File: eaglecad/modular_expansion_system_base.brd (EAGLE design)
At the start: 90.2 x 100 mm, 40 parts, among them IC1 74LS244N, IC10 74LS30N, IC2 74LS244N, IC3 74LS244N, IC4 SRAM, IC5 74LS30N, IC6 LM2596T-5.0, IC8 74LS00N, IC9 7805T, J1-INTERRUPTS INTERRUPTS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

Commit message: updated schematics, boards, and pdfs
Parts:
- renumbered LD1117 to LD1117V33
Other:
- board text added: "TRS80MXS Base - V1.2 Joe Rounceville (C) 2019"
- board text removed: "TRS80MXS Base - V1.1 Joe Rounceville (C) 2019"
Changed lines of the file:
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@@
 <text x="36.195" y="5.08" size="1.016" layer="25" font="fixed" ratio="6">D7</text>
 <text x="45.085" y="5.715" size="1.016" layer="25" font="fixed" ratio="6" rot="R90">RAS*</text>
-<text x="47.3075" y="5.715" size="1.016" layer="25" font="fixed" ratio="6" rot="R90">CAS*</text>
+<text x="47.3075" y="5.3975" size="1.016" layer="25" font="fixed" ratio="6" rot="R90">CAS*</text>
 <text x="49.8475" y="4.1275" size="0.6096" layer="25" font="fixed" ratio="6" rot="R90">RES*</text>
 <text x="53.6575" y="4.445" size="0.6096" layer="25" font="fixed" ratio="6" rot="R180">INTAK*</text>
@@
 <text x="60.0075" y="81.5975" size="0.6096" layer="25">4.7k</text>
 <text x="59.69" y="58.7375" size="0.6096" layer="25">4.7k</text>
-<text x="88.5825" y="28.8925" size="1.778" layer="25" rot="R90">TRS80MXS Base - V1.1
+<text x="88.5825" y="28.8925" size="1.778" layer="25" rot="R90">TRS80MXS Base - V1.2
 Joe Rounceville (C) 2019</text>
 </plain>
@@
 <attribute name="VALUE" x="51.308" y="5.842" size="0.6096" layer="27" ratio="10"/>
 </element>
-<element name="LD1117" library="SparkFun-IC-Power" library_urn="urn:adsk.eagle:library:526" package="78XXL" package3d_urn="urn:adsk.eagle:package:39065/1" value="V_REG_LD1117VXX" x="42.545" y="16.51" smashed="yes">
-<attribute name="NAME" x="38.735" y="21.59" size="1.778" layer="25" ratio="10"/>
+<element name="LD1117V33" library="SparkFun-IC-Power" library_urn="urn:adsk.eagle:library:526" package="78XXL" package3d_urn="urn:adsk.eagle:package:39065/1" value="V_REG_LD1117VXX" x="42.545" y="16.51" smashed="yes">
+<attribute name="NAME" x="36.195" y="20.955" size="1.778" layer="25" ratio="10"/>
 <attribute name="VALUE" x="38.608" y="19.685" size="0.6096" layer="27" ratio="10"/>
 </element>
@@
 <element name="IC6" library="linear" library_urn="urn:adsk.eagle:library:262" package="TO220-52" package3d_urn="urn:adsk.eagle:package:16443/1" value="LM2596T-5.0" x="48.895" y="26.035" smashed="yes" rot="R90">
 <attribute name="NAME" x="70.739" y="21.463" size="1.27" layer="25" rot="R180"/>
-<attribute name="VALUE" x="52.451" y="21.7805" size="1.27" layer="27"/>
+<attribute name="VALUE" x="52.7685" y="28.7655" size="1.27" layer="27"/>
 </element>
 <element name="C5" library="rcl" library_urn="urn:adsk.eagle:library:334" package="E2,5-5" package3d_urn="urn:adsk.eagle:package:23344/1" value="680uf" x="57.4675" y="17.4625" smashed="yes" rot="R90">
 <attribute name="NAME" x="56.1975" y="16.7005" size="1.27" layer="25" ratio="10" rot="R90"/>
 <attribute name="SPICEPREFIX" value="C" x="57.4675" y="17.4625" size="1.778" layer="27" rot="R90" display="off"/>
-<attribute name="VALUE" x="60.198" y="15.4305" size="1.27" layer="27" ratio="10" rot="R90"/>
+<attribute name="VALUE" x="59.563" y="15.748" size="1.016" layer="27" ratio="10" rot="R90"/>
 </element>
 <element name="D2-1N5824" library="diode" library_urn="urn:adsk.eagle:library:210" package="DO41-7.6" package3d_urn="urn:adsk.eagle:package:43421/1" value="1N5818-T" x="70.1675" y="37.1475" smashed="yes" rot="R90">
-<attribute name="NAME" x="69.1515" y="36.3855" size="1.27" layer="25" ratio="10" rot="R90"/>
-<attribute name="VALUE" x="70.5485" y="36.703" size="1.27" layer="27" ratio="10" rot="R90"/>
+<attribute name="NAME" x="68.834" y="34.4805" size="1.27" layer="25" ratio="10" rot="R90"/>
+<attribute name="VALUE" x="72.771" y="34.4805" size="1.27" layer="27" ratio="10" rot="R90"/>
 </element>
 <element name="L1" library="rcl" library_urn="urn:adsk.eagle:library:334" package="6000-XXXX-RC" package3d_urn="urn:adsk.eagle:package:23538/1" value="33uh" x="64.77" y="15.5575" smashed="yes">
@@
 <attribute name="NAME" x="49.8475" y="12.573" size="1.27" layer="25" ratio="10" rot="R90"/>
 <attribute name="SPICEPREFIX" value="C" x="51.7525" y="13.97" size="1.778" layer="27" rot="R90" display="off"/>
-<attribute name="VALUE" x="54.1655" y="11.938" size="1.27" layer="27" ratio="10" rot="R90"/>
+<attribute name="VALUE" x="53.848" y="12.2555" size="1.016" layer="27" ratio="10" rot="R90"/>
 </element>
 <element name="JP1" library="jumper" library_urn="urn:adsk.eagle:library:252" package="JP2" package3d_urn="urn:adsk.eagle:package:15452/1" value="5V_SOURCE" x="78.4225" y="30.48" smashed="yes" rot="R180">
-<attribute name="NAME" x="81.9785" y="28.829" size="1.27" layer="25" ratio="10" rot="R180"/>
-<attribute name="VALUE" x="81.9785" y="34.798" size="1.27" layer="27" ratio="10" rot="R180"/>
+<attribute name="NAME" x="73.0885" y="32.4485" size="1.27" layer="25" ratio="10" rot="R270"/>
+<attribute name="VALUE" x="83.8835" y="28.7655" size="1.27" layer="27" ratio="10" rot="R180"/>
 </element>
 </elements>
@@
 <contactref element="U$2" pad="1"/>
 <contactref element="J2_DATA_AND_POWER_CON" pad="2"/>
-<contactref element="LD1117" pad="IN"/>
+<contactref element="LD1117V33" pad="IN"/>
 <contactref element="C1" pad="-"/>
 <contactref element="IC1" pad="10"/>
@@
 <contactref element="R7" pad="1"/>
 <contactref element="C4" pad="+"/>
-<contactref element="LD1117" pad="OUT"/>
+<contactref element="LD1117V33" pad="OUT"/>
 <contactref element="JP1" pad="2"/>
 </signal>
@@
 <signal name="VCC/2">
 <contactref element="J2_DATA_AND_POWER_CON" pad="3"/>
-<contactref element="LD1117" pad="GND"/>
+<contactref element="LD1117V33" pad="GND"/>
 <contactref element="C1" pad="+"/>
 <wire x1="50.93739375" y1="4.7024" x2="49.5476" y2="4.7024" width="0.3" layer="16"/>

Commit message: added bill of materials
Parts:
- removed C5: 680uf, rcl:E2,5-5
- added C13: 680uf, rcl:E3,5-8
- moved IC6 1.59 mm to (48.9, 27.6)
- moved C9 0.63 mm to (51.1, 14.0)
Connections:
- net 9V-POST-SW: now also C13.+; no longer C5.+
- net GND: now also C13.-; no longer C5.-
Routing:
- net 9V-POST-SW: track 51.3 -> 57.3 mm
- net 5V_FROM_SWITCHER: track 44.9 -> 49.5 mm
- net N$1: track 25.7 -> 26.3 mm
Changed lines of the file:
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@@
 <attribute name="VALUE" x="70.612" y="93.6625" size="0.6096" layer="27" font="vector" ratio="20" rot="R270"/>
 </element>
-<element name="IC6" library="linear" library_urn="urn:adsk.eagle:library:262" package="TO220-52" package3d_urn="urn:adsk.eagle:package:16443/1" value="LM2596T-5.0" x="48.895" y="26.035" smashed="yes" rot="R90">
-<attribute name="NAME" x="70.739" y="21.463" size="1.27" layer="25" rot="R180"/>
-<attribute name="VALUE" x="52.7685" y="28.7655" size="1.27" layer="27"/>
-</element>
-<element name="C5" library="rcl" library_urn="urn:adsk.eagle:library:334" package="E2,5-5" package3d_urn="urn:adsk.eagle:package:23344/1" value="680uf" x="57.4675" y="17.4625" smashed="yes" rot="R90">
-<attribute name="NAME" x="56.1975" y="16.7005" size="1.27" layer="25" ratio="10" rot="R90"/>
-<attribute name="SPICEPREFIX" value="C" x="57.4675" y="17.4625" size="1.778" layer="27" rot="R90" display="off"/>
-<attribute name="VALUE" x="59.563" y="15.748" size="1.016" layer="27" ratio="10" rot="R90"/>
+<element name="IC6" library="linear" library_urn="urn:adsk.eagle:library:262" package="TO220-52" package3d_urn="urn:adsk.eagle:package:16443/1" value="LM2596T-5.0" x="48.895" y="27.6225" smashed="yes" rot="R90">
+<attribute name="NAME" x="70.739" y="23.0505" size="1.27" layer="25" rot="R180"/>
+<attribute name="VALUE" x="55.3085" y="27.4955" size="1.27" layer="27"/>
 </element>
 <element name="D2-1N5824" library="diode" library_urn="urn:adsk.eagle:library:210" package="DO41-7.6" package3d_urn="urn:adsk.eagle:package:43421/1" value="1N5818-T" x="70.1675" y="37.1475" smashed="yes" rot="R90">
@@
 <attribute name="VALUE" x="62.8044" y="13.2744" size="1.27" layer="27"/>
 </element>
-<element name="C9" library="rcl" library_urn="urn:adsk.eagle:library:334" package="E2,5-5" package3d_urn="urn:adsk.eagle:package:23344/1" value="220uf" x="51.7525" y="13.97" smashed="yes" rot="R90">
-<attribute name="NAME" x="49.8475" y="12.573" size="1.27" layer="25" ratio="10" rot="R90"/>
-<attribute name="SPICEPREFIX" value="C" x="51.7525" y="13.97" size="1.778" layer="27" rot="R90" display="off"/>
-<attribute name="VALUE" x="53.848" y="12.2555" size="1.016" layer="27" ratio="10" rot="R90"/>
+<element name="C9" library="rcl" library_urn="urn:adsk.eagle:library:334" package="E2,5-5" package3d_urn="urn:adsk.eagle:package:23344/1" value="220uf" x="51.1175" y="13.97" smashed="yes" rot="R90">
+<attribute name="NAME" x="49.2125" y="12.573" size="1.27" layer="25" ratio="10" rot="R90"/>
+<attribute name="SPICEPREFIX" value="C" x="51.1175" y="13.97" size="1.778" layer="27" rot="R90" display="off"/>
+<attribute name="VALUE" x="53.213" y="12.2555" size="1.016" layer="27" ratio="10" rot="R90"/>
 </element>
 <element name="JP1" library="jumper" library_urn="urn:adsk.eagle:library:252" package="JP2" package3d_urn="urn:adsk.eagle:package:15452/1" value="5V_SOURCE" x="78.4225" y="30.48" smashed="yes" rot="R180">
 <attribute name="NAME" x="73.0885" y="32.4485" size="1.27" layer="25" ratio="10" rot="R270"/>
 <attribute name="VALUE" x="83.8835" y="28.7655" size="1.27" layer="27" ratio="10" rot="R180"/>
+</element>
+<element name="C13" library="rcl" library_urn="urn:adsk.eagle:library:334" package="E3,5-8" package3d_urn="urn:adsk.eagle:package:23360/2" value="680uf" x="56.515" y="17.78" smashed="yes">
+<attribute name="NAME" x="59.817" y="20.574" size="1.27" layer="25" ratio="10"/>
+<attribute name="SPICEPREFIX" value="C" x="56.515" y="17.78" size="1.778" layer="27" display="off"/>
+<attribute name="VALUE" x="54.229" y="14.732" size="1.27" layer="27" ratio="10"/>
 </element>
 </elements>
@@
 <contactref element="IC6" pad="3"/>
 <contactref element="IC6" pad="5"/>
-<contactref element="C5" pad="-"/>
 <contactref element="D2-1N5824" pad="A"/>
 <contactref element="C9" pad="-"/>
+<contactref element="C13" pad="-"/>
 </signal>
 <signal name="VCC">
@@
 <contactref element="J2_DATA_AND_POWER_CON" pad="4"/>
 <contactref element="IC6" pad="1"/>
-<contactref element="C5" pad="+"/>
 <wire x1="73.66" y1="16.7894" x2="69.995" y2="20.4544" width="0.508" layer="1"/>
-<wire x1="69.995" y1="20.4544" x2="69.995" y2="22.635" width="0.508" layer="1"/>
 <wire x1="59.69" y1="2.54" x2="58.42" y2="3.81" width="0.508" layer="1"/>
 <wire x1="58.42" y1="3.81" x2="58.42" y2="7.62" width="0.508" layer="1"/>
-<wire x1="58.42" y1="7.62" x2="57.4675" y2="8.5725" width="0.508" layer="1"/>
-<wire x1="57.4675" y1="8.5725" x2="57.4675" y2="16.1925" width="0.508" layer="1"/>
-<wire x1="57.4675" y1="16.1925" x2="61.7294" y2="20.4544" width="0.508" layer="1"/>
-<wire x1="61.7294" y1="20.4544" x2="69.995" y2="20.4544" width="0.508" layer="1"/>
-<wire x1="73.50125" y1="32.86125" x2="75.8825" y2="35.2425" width="0.508" layer="1"/>
-<wire x1="72.1269" y1="24.94005625" x2="69.995" y2="22.80815625" width="0.508" layer="1"/>
-<wire x1="69.995" y1="22.635" x2="69.995" y2="22.80815625" width="0.508" layer="1"/>
-<wire x1="72.1269" y1="24.94005625" x2="72.1269" y2="27.6225" width="0.508" layer="1"/>
-<wire x1="72.1269" y1="27.6225" x2="73.50125" y2="28.99685" width="0.508" layer="1"/>
-<wire x1="73.50125" y1="28.99685" x2="73.50125" y2="32.86125" width="0.508" layer="1"/>
+<contactref element="C13" pad="+"/>
+<wire x1="75.8825" y1="35.2425" x2="73.3425" y2="32.7025" width="0.508" layer="1"/>
+<wire x1="73.3425" y1="27.57" x2="69.995" y2="24.2225" width="0.508" layer="1"/>
+<wire x1="73.3425" y1="32.7025" x2="73.3425" y2="27.57" width="0.508" layer="1"/>
+<wire x1="69.995" y1="20.4544" x2="55.3794" y2="20.4544" width="0.508" layer="1"/>
+<wire x1="55.3794" y1="20.4544" x2="54.737" y2="19.812" width="0.508" layer="1"/>
+<wire x1="54.737" y1="19.812" x2="54.737" y2="17.78" width="0.508" layer="1"/>
+<wire x1="54.737" y1="11.303" x2="54.737" y2="17.78" width="0.508" layer="1"/>
+<wire x1="58.42" y1="7.62" x2="54.737" y2="11.303" width="0.508" layer="1"/>
+<wire x1="69.995" y1="24.2225" x2="69.995" y2="20.4544" width="0.508" layer="1"/>
 </signal>
 <signal name="N$20">
@@
 <contactref element="IC6" pad="2"/>
 <contactref element="L1" pad="1"/>
-<wire x1="67.365" y1="24.335" x2="64.5075" y2="24.335" width="0.508" layer="16"/>
-<wire x1="64.5075" y1="24.335" x2="62.27" y2="22.0975" width="0.508" layer="16"/>
 <wire x1="62.27" y1="15.5575" x2="62.27" y2="22.0975" width="0.508" layer="16"/>
-<wire x1="65.0875" y1="28.2575" x2="65.0875" y2="24.765" width="0.508" layer="1"/>
-<wire x1="65.5175" y1="24.335" x2="67.365" y2="24.335" width="0.508" layer="1"/>
-<wire x1="65.0875" y1="24.765" x2="65.5175" y2="24.335" width="0.508" layer="1"/>
-<wire x1="70.1675" y1="33.3375" x2="65.0875" y2="28.2575" width="0.508" layer="1"/>
+<wire x1="70.1675" y1="33.3375" x2="67.945" y2="33.3375" width="0.508" layer="16"/>
+<wire x1="67.945" y1="33.3375" x2="65.0875" y2="30.48" width="0.508" layer="16"/>
+<wire x1="65.0875" y1="30.48" x2="65.0875" y2="26.035" width="0.508" layer="16"/>
+<wire x1="65.0875" y1="26.035" x2="67.2525" y2="26.035" width="0.508" layer="16"/>
+<wire x1="67.2525" y1="26.035" x2="67.365" y2="25.9225" width="0.508" layer="16"/>
+<wire x1="62.27" y1="22.0975" x2="66.095" y2="25.9225" width="0.508" layer="16"/>
+<wire x1="66.095" y1="25.9225" x2="67.365" y2="25.9225" width="0.508" layer="16"/>
 </signal>
 <signal name="5V_FROM_SWITCHER">
@@
 <wire x1="67.27" y1="15.5575" x2="67.27" y2="11.03946875" width="0.508" layer="16"/>
 <wire x1="67.27" y1="11.03946875" x2="66.54293125" y2="10.3124" width="0.508" layer="16"/>
-<wire x1="70.52394375" y1="27.7804" x2="71.8094" y2="26.49494375" width="0.508" layer="16"/>
-<wire x1="70.52394375" y1="27.7804" x2="67.4104" y2="27.7804" width="0.508" layer="16"/>
-<wire x1="67.365" y1="27.735" x2="67.4104" y2="27.7804" width="0.508" layer="16"/>
-<wire x1="71.8094" y1="26.49494375" x2="71.8094" y2="20.0969" width="0.508" layer="16"/>
-<wire x1="71.8094" y1="20.0969" x2="67.27" y2="15.5575" width="0.508" layer="16"/>
+<wire x1="67.365" y1="29.3225" x2="67.4104" y2="29.3679" width="0.508" layer="16"/>
 <wire x1="75.8825" y1="30.48" x2="71.89744375" y2="26.49494375" width="0.508" layer="16"/>
-<wire x1="71.89744375" y1="26.49494375" x2="71.8094" y2="26.49494375" width="0.508" layer="16"/>
-<wire x1="54.1401" y1="10.3124" x2="51.7525" y2="12.7" width="0.508" layer="16"/>
-<wire x1="66.54293125" y1="10.3124" x2="54.1401" y2="10.3124" width="0.508" layer="16"/>
+<wire x1="53.5051" y1="10.3124" x2="51.1175" y2="12.7" width="0.508" layer="16"/>
+<wire x1="66.54293125" y1="10.3124" x2="53.5051" y2="10.3124" width="0.508" layer="16"/>
+<wire x1="74.725" y1="29.3225" x2="75.8825" y2="30.48" width="0.508" layer="16"/>
+<wire x1="67.365" y1="29.3225" x2="74.725" y2="29.3225" width="0.508" layer="16"/>
+<wire x1="71.89744375" y1="26.49494375" x2="71.89744375" y2="20.18494375" width="0.508" layer="16"/>
+<wire x1="71.89744375" y1="20.18494375" x2="67.27" y2="15.5575" width="0.508" layer="16"/>
 </signal>
 <signal name="5V_FROM_LINEAR_REG">

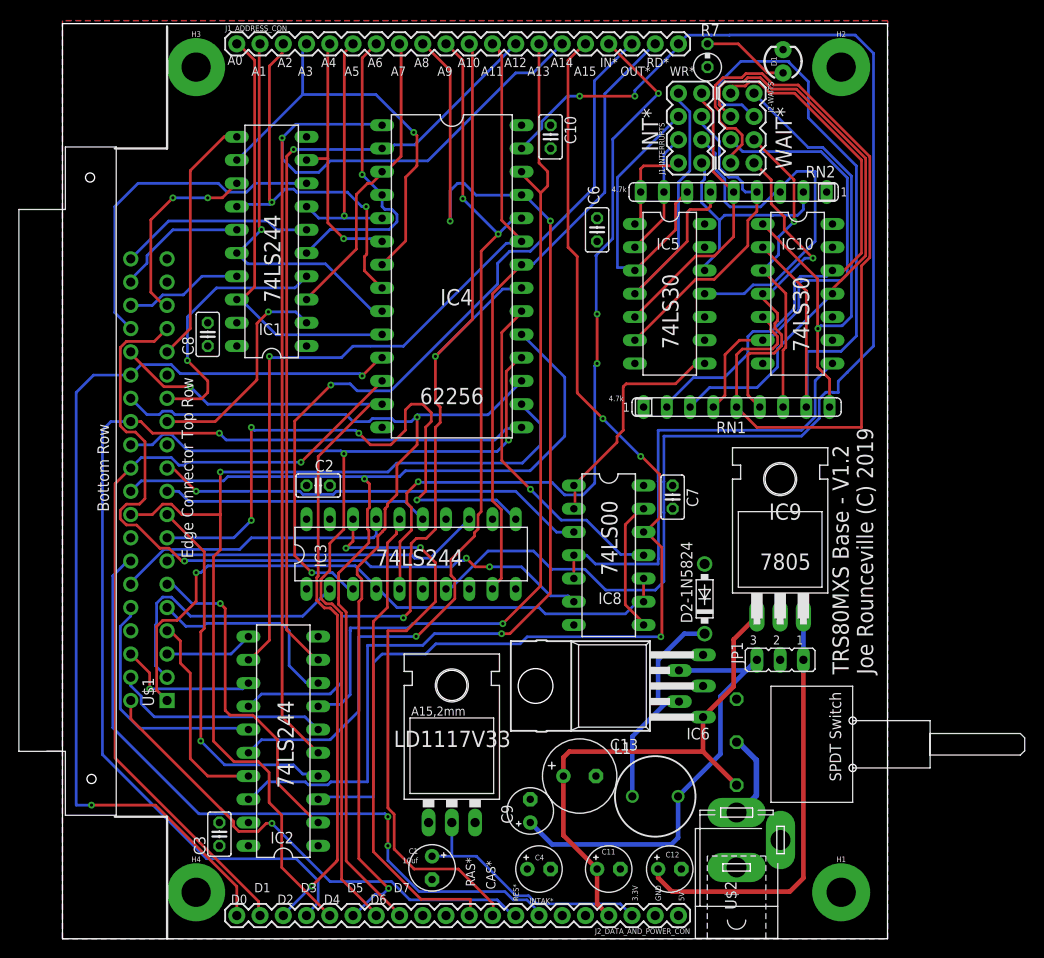
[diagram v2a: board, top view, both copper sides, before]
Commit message: implemented pacman fruit behavior
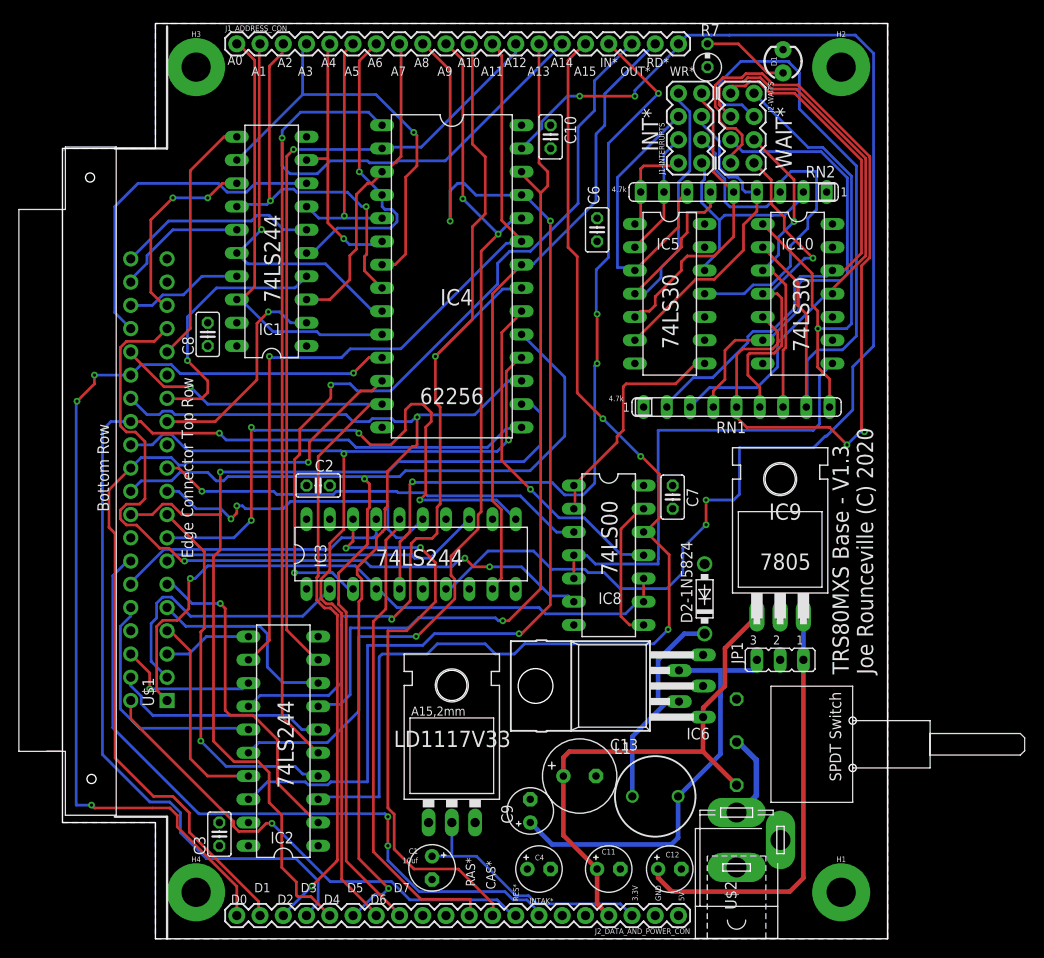
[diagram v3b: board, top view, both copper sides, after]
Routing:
- net IN*: track 29.2 -> 35.0 mm, vias 0 -> 2
- net D1: track 88.3 -> 91.3 mm
- net WAIT4*: track 90.8 -> 93.7 mm, vias 0 -> 2
- net BUFFERED_WR*: track 150.0 -> 147.4 mm, vias 2 -> 4
- net BUFFERED_A14: track 119.7 -> 122.0 mm
- net 5V_FROM_SWITCHER: track 49.5 -> 47.2 mm
- net BUFFERED_A15: track 125.7 -> 127.6 mm
- net D3: track 116.6 -> 118.6 mm
- net D4: track 107.9 -> 109.4 mm
- net BUFFERED_A7: track 32.9 -> 34.4 mm
- net RAS: track 14.6 -> 15.9 mm
- net BUFFERED_OUT*: track 85.3 -> 86.4 mm
- net INT3*: track 31.6 -> 32.7 mm
- net BUFFERED_A10: track 105.0 -> 106.1 mm
- net INT0*: track 25.1 -> 24.2 mm
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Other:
- outline, holes or cut-outs redrawn
- board text added: "TRS80MXS Base - V1.3 Joe Rounceville (C) 2020"
- board text removed: "TRS80MXS Base - V1.2 Joe Rounceville (C) 2019"
